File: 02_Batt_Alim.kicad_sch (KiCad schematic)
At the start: 26 parts

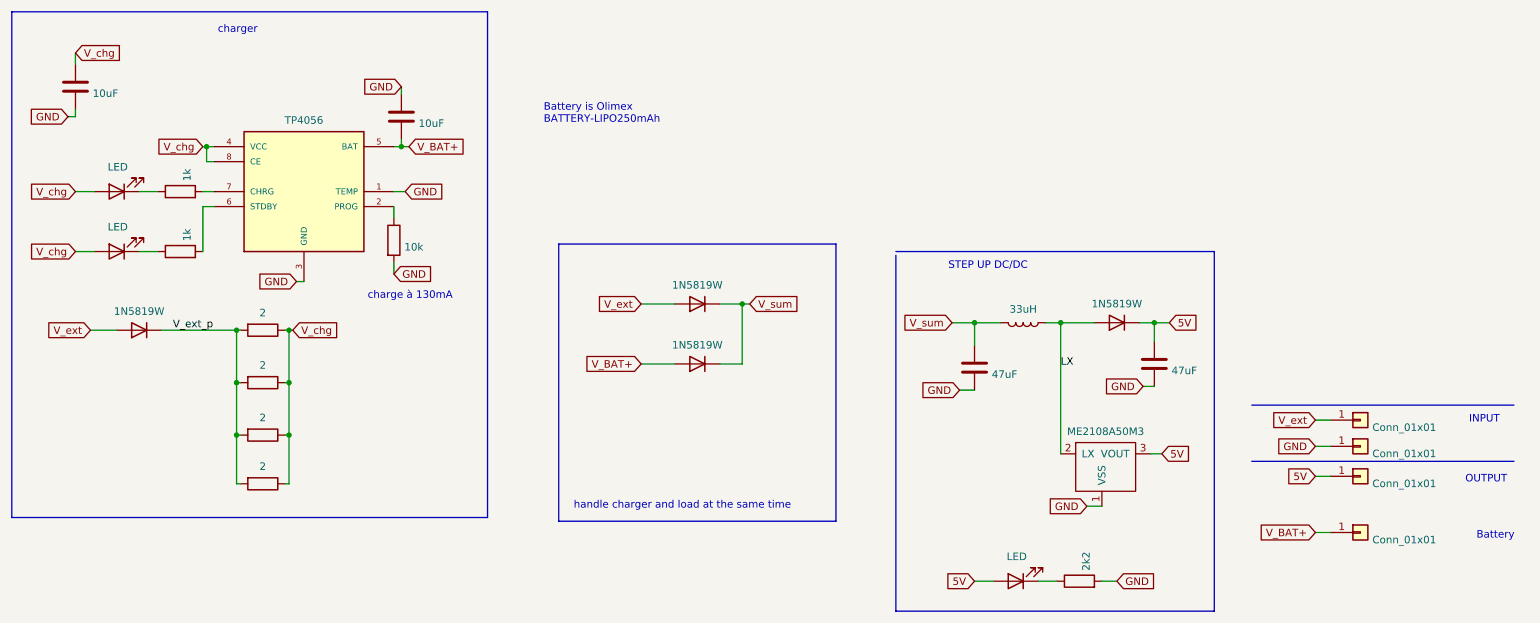
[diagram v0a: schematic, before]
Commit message: maj schéma avec champ lcsc
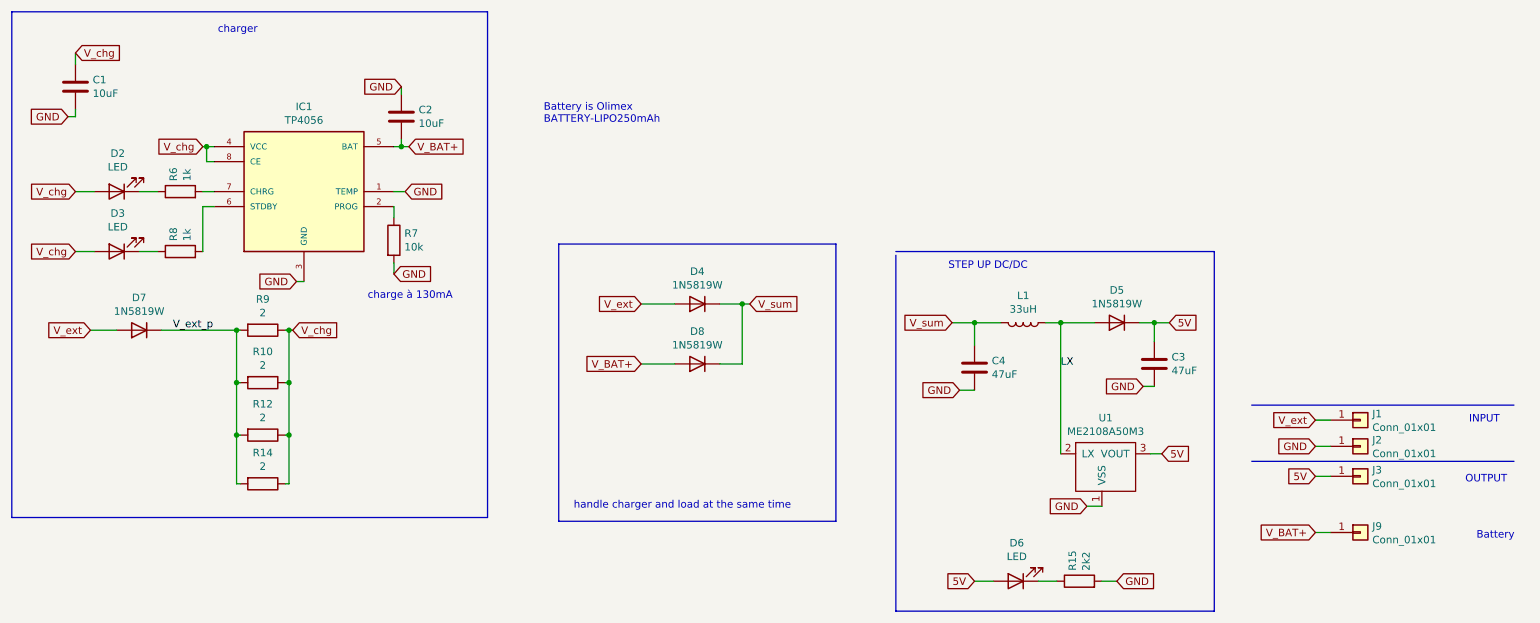
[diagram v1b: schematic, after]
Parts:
- C1, C2: renamed from ?; LCSC (none) -> C19702
- C3, C4: renamed from ?; LCSC (none) -> C77101
- D2, D3, D6: renamed from ?; LCSC (none) -> C2286
- D4, D5, D7, D8: renamed from ?; LCSC (none) -> C369930
- IC1: renamed from ?; LCSC (none) -> C16581
- L1: renamed from ?; LCSC (none) -> C9936
- R10, R12, R14, R9: renamed from ?; LCSC (none) -> C22977
- R15: renamed from ?; LCSC (none) -> C4190
- R6, R8: renamed from ?; LCSC (none) -> C21190
- R7: renamed from ?; LCSC (none) -> C22765
- U1: renamed from ?; LCSC (none) -> C14839
- gave numbers to parts that had none: 4

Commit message: maj schema retouche placement et routage fabrication
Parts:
- D4, D5, D7, D8: value 1N5819W -> SS14; footprint Diode_SMD:D_SOD-123F -> Diode_SMD:D_SMA; LCSC C369930 -> C2480
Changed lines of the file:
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@@
     (pin "1")
-  )
-  (symbol (lib_id "Device:D") (at 136.525 85.725 180) (unit 1)
-    (in_bom yes) (on_board yes)
-    (property "Reference" "D4" (id 0) (at 136.525 80.2132 0))
-    (property "Value" "1N5819W" (id 1) (at 136.525 82.5246 0))
-    (property "Footprint" "Diode_SMD:D_SOD-123F" (id 2) (at 136.525 85.725 0)
-      (effects (font (size 1.27 1.27)) hide)
-    )
-    (property "Datasheet" "-" (id 3) (at 136.525 85.725 0)
-      (effects (font (size 1.27 1.27)) hide)
-    )
-    (property "LCSC" "C369930" (id 4) (at 136.525 85.725 0)
-      (effects (font (size 1.27 1.27)) hide)
-    )
-    (pin "1")
-    (pin "2")
-  )
-  (symbol (lib_id "Device:D") (at 41.91 90.17 180) (unit 1)
-    (in_bom yes) (on_board yes)
-    (property "Reference" "D7" (id 0) (at 41.91 84.6582 0))
-    (property "Value" "1N5819W" (id 1) (at 41.91 86.9696 0))
-    (property "Footprint" "Diode_SMD:D_SOD-123F" (id 2) (at 41.91 90.17 0)
-      (effects (font (size 1.27 1.27)) hide)
-    )
-    (property "Datasheet" "-" (id 3) (at 41.91 90.17 0)
-      (effects (font (size 1.27 1.27)) hide)
-    )
-    (property "LCSC" "C369930" (id 4) (at 41.91 90.17 0)
-      (effects (font (size 1.27 1.27)) hide)
-    )
-    (pin "1")
-    (pin "2")
-  )
-  (symbol (lib_id "Device:D") (at 136.525 95.885 180) (unit 1)
-    (in_bom yes) (on_board yes)
-    (property "Reference" "D8" (id 0) (at 136.525 90.3732 0))
-    (property "Value" "1N5819W" (id 1) (at 136.525 92.6846 0))
-    (property "Footprint" "Diode_SMD:D_SOD-123F" (id 2) (at 136.525 95.885 0)
-      (effects (font (size 1.27 1.27)) hide)
-    )
-    (property "Datasheet" "-" (id 3) (at 136.525 95.885 0)
-      (effects (font (size 1.27 1.27)) hide)
-    )
-    (property "LCSC" "C369930" (id 4) (at 136.525 95.885 0)
-      (effects (font (size 1.27 1.27)) hide)
-    )
-    (pin "1")
-    (pin "2")
   )
   (symbol (lib_id "Device:LED") (at 190.5 132.715 180) (unit 1)
@@
     )
     (property "LCSC" "C2286" (id 4) (at 190.5 132.715 0)
-      (effects (font (size 1.27 1.27)) hide)
-    )
-    (pin "1")
-    (pin "2")
-  )
-  (symbol (lib_id "Device:D") (at 207.645 88.9 180) (unit 1)
-    (in_bom yes) (on_board yes)
-    (property "Reference" "D5" (id 0) (at 207.645 83.3882 0))
-    (property "Value" "1N5819W" (id 1) (at 207.645 85.6996 0))
-    (property "Footprint" "Diode_SMD:D_SOD-123F" (id 2) (at 207.645 88.9 0)
-      (effects (font (size 1.27 1.27)) hide)
-    )
-    (property "Datasheet" "-" (id 3) (at 207.645 88.9 0)
-      (effects (font (size 1.27 1.27)) hide)
-    )
-    (property "LCSC" "C369930" (id 4) (at 207.645 88.9 0)
       (effects (font (size 1.27 1.27)) hide)
     )
@@
     (pin "1")
   )
+  (symbol (lib_id "Device:D") (at 136.525 85.725 180) (unit 1)
+    (in_bom yes) (on_board yes)
+    (property "Reference" "D4" (id 0) (at 136.525 80.2132 0))
+    (property "Value" "SS14" (id 1) (at 136.525 82.5246 0))
+    (property "Footprint" "Diode_SMD:D_SMA" (id 2) (at 136.525 85.725 0)
+      (effects (font (size 1.27 1.27)) hide)
+    )
+    (property "Datasheet" "-" (id 3) (at 136.525 85.725 0)
+      (effects (font (size 1.27 1.27)) hide)
+    )
+    (property "LCSC" "C2480" (id 4) (at 136.525 85.725 0)
+      (effects (font (size 1.27 1.27)) hide)
+    )
+    (pin "1")
+    (pin "2")
+  )
+  (symbol (lib_id "Device:D") (at 207.645 88.9 180) (unit 1)
+    (in_bom yes) (on_board yes)
+    (property "Reference" "D5" (id 0) (at 207.645 83.3882 0))
+    (property "Value" "SS14" (id 1) (at 207.645 85.6996 0))
+    (property "Footprint" "Diode_SMD:D_SMA" (id 2) (at 207.645 88.9 0)
+      (effects (font (size 1.27 1.27)) hide)
+    )
+    (property "Datasheet" "-" (id 3) (at 207.645 88.9 0)
+      (effects (font (size 1.27 1.27)) hide)
+    )
+    (property "LCSC" "C2480" (id 4) (at 207.645 88.9 0)
+      (effects (font (size 1.27 1.27)) hide)
+    )
+    (pin "1")
+    (pin "2")
+  )
+  (symbol (lib_id "Device:D") (at 136.525 95.885 180) (unit 1)
+    (in_bom yes) (on_board yes)
+    (property "Reference" "D8" (id 0) (at 136.525 90.3732 0))
+    (property "Value" "SS14" (id 1) (at 136.525 92.6846 0))
+    (property "Footprint" "Diode_SMD:D_SMA" (id 2) (at 136.525 95.885 0)
+      (effects (font (size 1.27 1.27)) hide)
+    )
+    (property "Datasheet" "-" (id 3) (at 136.525 95.885 0)
+      (effects (font (size 1.27 1.27)) hide)
+    )
+    (property "LCSC" "C2480" (id 4) (at 136.525 95.885 0)
+      (effects (font (size 1.27 1.27)) hide)
+    )
+    (pin "1")
+    (pin "2")
+  )
+  (symbol (lib_id "Device:D") (at 41.91 90.17 180) (unit 1)
+    (in_bom yes) (on_board yes)
+    (property "Reference" "D7" (id 0) (at 41.91 84.6582 0))
+    (property "Value" "SS14" (id 1) (at 41.91 86.9696 0))
+    (property "Footprint" "Diode_SMD:D_SMA" (id 2) (at 41.91 90.17 0)
+      (effects (font (size 1.27 1.27)) hide)
+    )
+    (property "Datasheet" "-" (id 3) (at 41.91 90.17 0)
+      (effects (font (size 1.27 1.27)) hide)
+    )
+    (property "LCSC" "C2480" (id 4) (at 41.91 90.17 0)
+      (effects (font (size 1.27 1.27)) hide)
+    )
+    (pin "1")
+    (pin "2")
+  )
   (sheet_instances
     (path "/" (page "1"))
@@
       (reference "D3") (unit 1) (value "LED") (footprint "Diode_SMD:D_0603_1608Metric")
     )
-    (path "/00000000-0000-0000-0000-00005fda974e"
-      (reference "D4") (unit 1) (value "1N5819W") (footprint "Diode_SMD:D_SOD-123F")
+    (path "/73c6a22d-8e24-4104-9b12-2a9e25e4c916"
+      (reference "D4") (unit 1) (value "SS14") (footprint "Diode_SMD:D_SMA")
     )
-    (path "/00000000-0000-0000-0000-00005fdd39f1"
-      (reference "D5") (unit 1) (value "1N5819W") (footprint "Diode_SMD:D_SOD-123F")
+    (path "/a9d9459a-1bb8-40c1-997e-b998ea134461"
+      (reference "D5") (unit 1) (value "SS14") (footprint "Diode_SMD:D_SMA")
     )
     (path "/00000000-0000-0000-0000-00005fdb7451"
       (reference "D6") (unit 1) (value "LED") (footprint "Diode_SMD:D_0603_1608Metric")
     )
-    (path "/00000000-0000-0000-0000-00005fdb60ba"
-      (reference "D7") (unit 1) (value "1N5819W") (footprint "Diode_SMD:D_SOD-123F")
+    (path "/d5aa261e-d3f2-4c4f-afc2-83a41d85686c"
+      (reference "D7") (unit 1) (value "SS14") (footprint "Diode_SMD:D_SMA")
     )
-    (path "/00000000-0000-0000-0000-00005fdb69c2"
-      (reference "D8") (unit 1) (value "1N5819W") (footprint "Diode_SMD:D_SOD-123F")
+    (path "/c0e89f69-707b-4e9a-ba56-d7943731c229"
+      (reference "D8") (unit 1) (value "SS14") (footprint "Diode_SMD:D_SMA")
     )
     (path "/00000000-0000-0000-0000-00005fd80f7f"
